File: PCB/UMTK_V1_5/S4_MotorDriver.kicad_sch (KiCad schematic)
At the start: 17 parts, among them J2 Motor Out, J3 Motor Shunt, U6 DRV8873SPWPRQ1

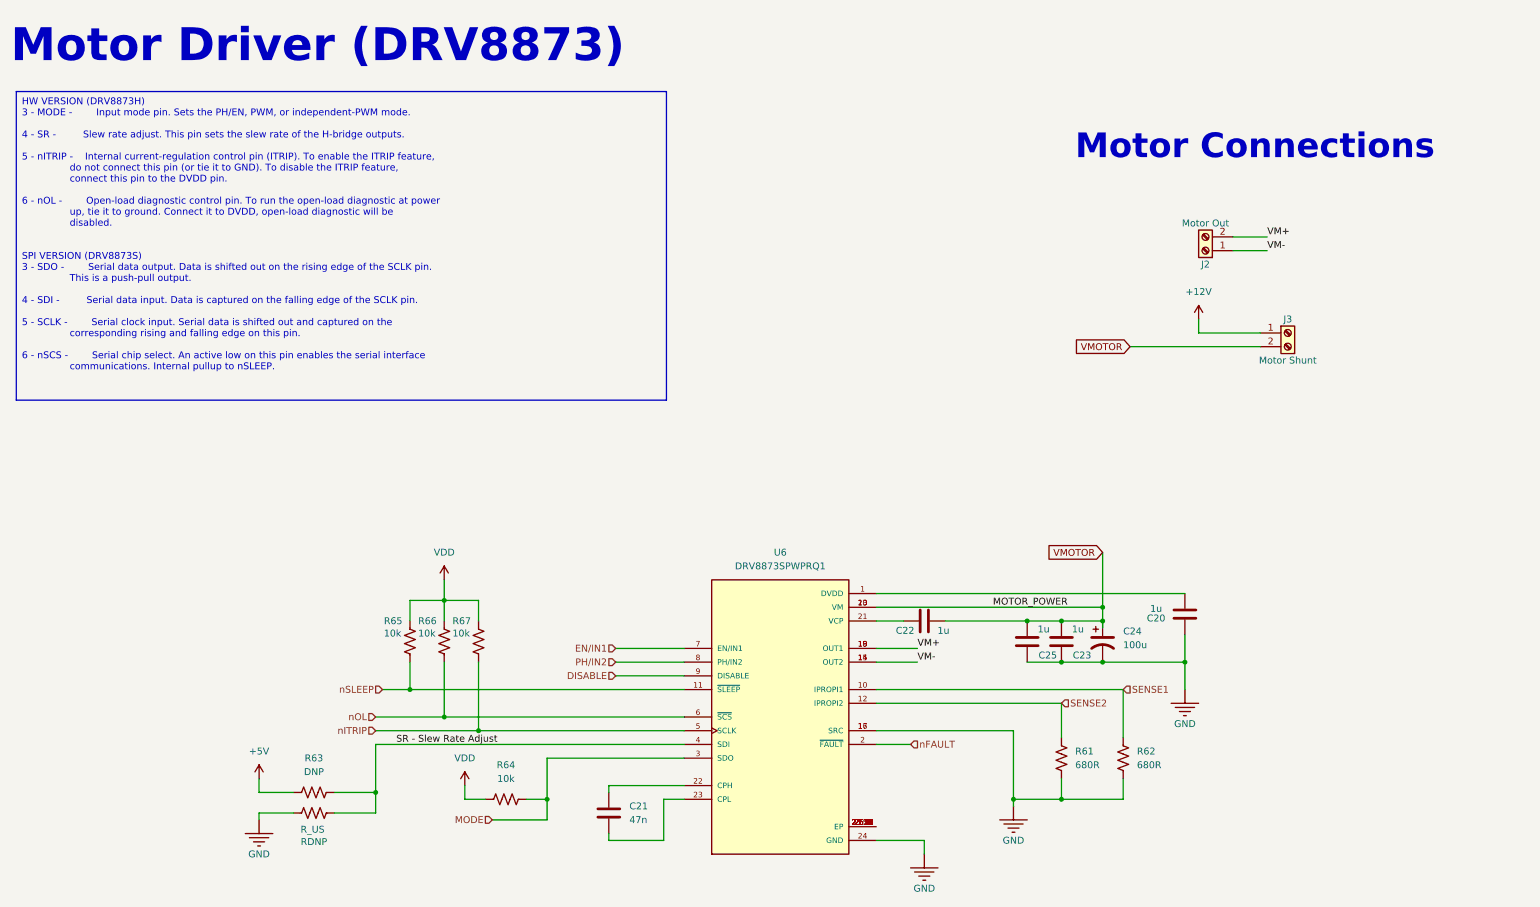
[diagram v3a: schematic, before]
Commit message: Schematic Done, Assigning footprint
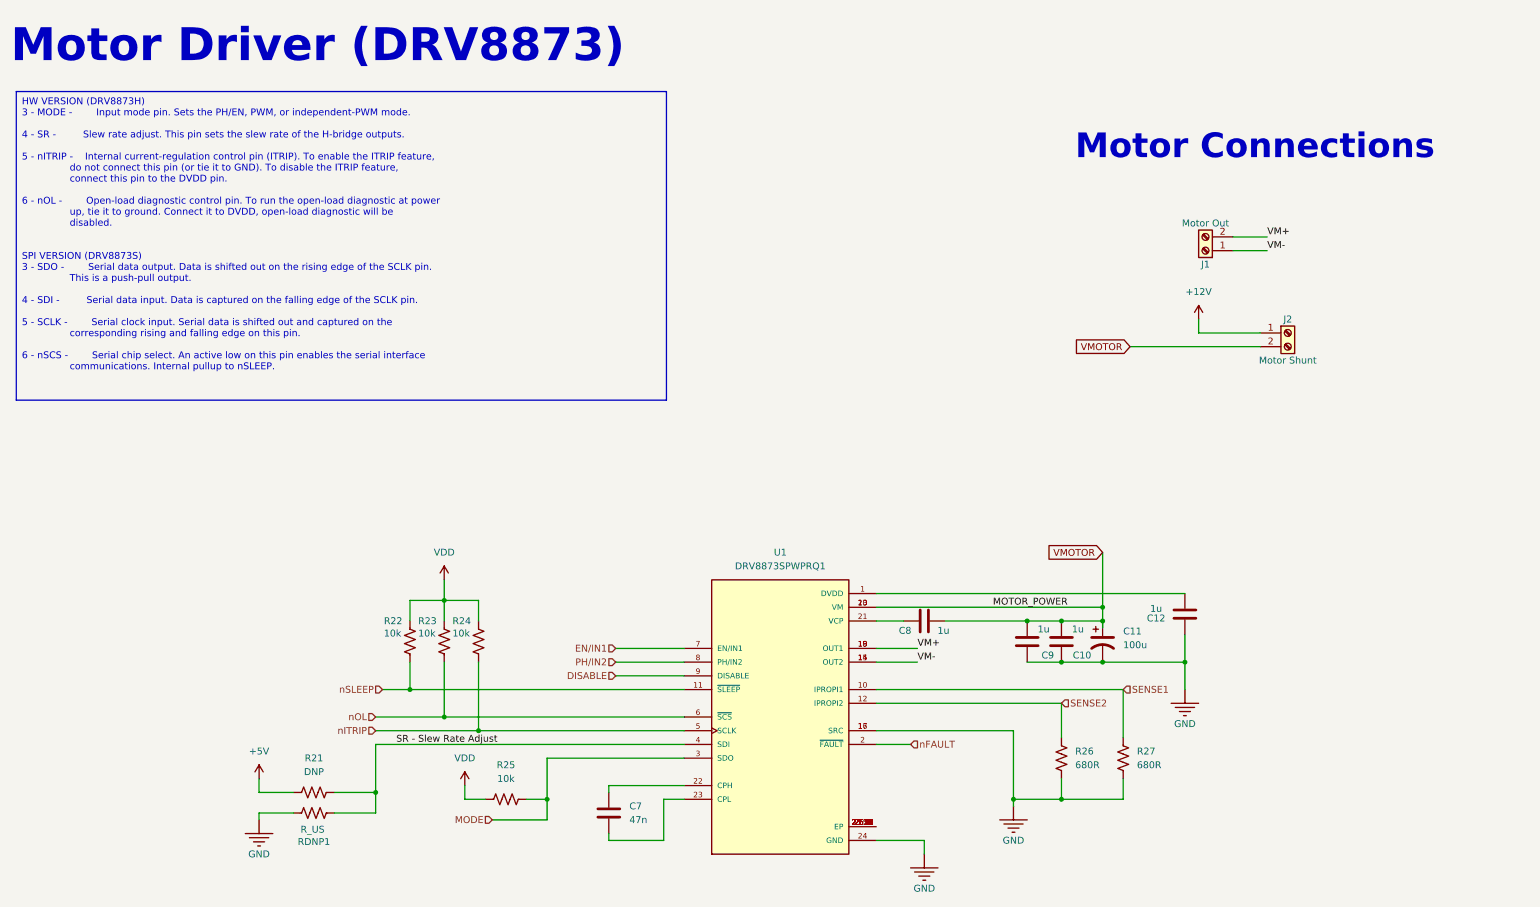
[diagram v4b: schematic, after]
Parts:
- renumbered C23 to C10, C24 to C11, C20 to C12, C21 to C7, C22 to C8, C25 to C9, J2 to J1, J3 to J2, R63 to R21, R65 to R22, R66 to R23, R67 to R24, R64 to R25, R61 to R26, R62 to R27, RDNP to RDNP1, U6 to U1
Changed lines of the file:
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@@
 		(dnp no)
 		(fields_autoplaced yes)
-		(property "Reference" "U6"
+		(property "Reference" "U1"
 			(at 156.21 110.49 0)
 			(effects
@@
 			(project ""
 				(path "/2bf3ea67-58b8-47b3-a768-ea6950b40edf/429db1c7-ec58-4147-903c-f97ceea1f1c2"
-					(reference "U6")
+					(reference "U1")
 					(unit 1)
 				)
@@
 		(dnp no)
 		(fields_autoplaced yes)
-		(property "Reference" "C21"
+		(property "Reference" "C7"
 			(at 128.27 157.4799 0)
 			(effects
@@
 			(project ""
 				(path "/2bf3ea67-58b8-47b3-a768-ea6950b40edf/429db1c7-ec58-4147-903c-f97ceea1f1c2"
-					(reference "C21")
+					(reference "C7")
 					(unit 1)
 				)
@@
 		(dnp no)
 		(fields_autoplaced yes)
-		(property "Reference" "R63"
+		(property "Reference" "R21"
 			(at 69.85 148.59 90)
 			(effects
@@
 			(project "UMTK"
 				(path "/2bf3ea67-58b8-47b3-a768-ea6950b40edf/429db1c7-ec58-4147-903c-f97ceea1f1c2"
-					(reference "R63")
+					(reference "R21")
 					(unit 1)
 				)
@@
 		(on_board yes)
 		(dnp no)
-		(property "Reference" "#PWR0160"
+		(property "Reference" "#PWR027"
 			(at 199.39 157.48 0)
 			(effects
@@
 			(project "UMTK"
 				(path "/2bf3ea67-58b8-47b3-a768-ea6950b40edf/429db1c7-ec58-4147-903c-f97ceea1f1c2"
-					(reference "#PWR0160")
+					(reference "#PWR027")
 					(unit 1)
 				)
@@
 		(dnp no)
 		(fields_autoplaced yes)
-		(property "Reference" "#PWR0140"
+		(property "Reference" "#PWR029"
 			(at 233.68 71.12 0)
 			(effects
@@
 			(project "UMTK"
 				(path "/2bf3ea67-58b8-47b3-a768-ea6950b40edf/429db1c7-ec58-4147-903c-f97ceea1f1c2"
-					(reference "#PWR0140")
+					(reference "#PWR029")
 					(unit 1)
 				)
@@
 		(on_board yes)
 		(dnp no)
-		(property "Reference" "C20"
+		(property "Reference" "C12"
 			(at 225.806 122.682 0)
 			(effects
@@
 			(project "UMTK"
 				(path "/2bf3ea67-58b8-47b3-a768-ea6950b40edf/429db1c7-ec58-4147-903c-f97ceea1f1c2"
-					(reference "C20")
+					(reference "C12")
 					(unit 1)
 				)
@@
 		(dnp no)
 		(fields_autoplaced yes)
-		(property "Reference" "R61"
+		(property "Reference" "R26"
 			(at 210.82 147.3199 0)
 			(effects
@@
 			(project ""
 				(path "/2bf3ea67-58b8-47b3-a768-ea6950b40edf/429db1c7-ec58-4147-903c-f97ceea1f1c2"
-					(reference "R61")
+					(reference "R26")
 					(unit 1)
 				)
@@
 		(on_board yes)
 		(dnp no)
-		(property "Reference" "J2"
+		(property "Reference" "J1"
 			(at 234.95 57.15 0)
 			(effects
@@
 			(project "UMTK"
 				(path "/2bf3ea67-58b8-47b3-a768-ea6950b40edf/429db1c7-ec58-4147-903c-f97ceea1f1c2"
-					(reference "J2")
+					(reference "J1")
 					(unit 1)
 				)
@@
 		(on_board yes)
 		(dnp no)
-		(property "Reference" "C25"
+		(property "Reference" "C9"
 			(at 205.74 129.54 0)
 			(effects
@@
 			(project "UMTK"
 				(path "/2bf3ea67-58b8-47b3-a768-ea6950b40edf/429db1c7-ec58-4147-903c-f97ceea1f1c2"
-					(reference "C25")
+					(reference "C9")
 					(unit 1)
 				)
@@
 		(dnp no)
 		(fields_autoplaced yes)
-		(property "Reference" "#PWR039"
+		(property "Reference" "#PWR024"
 			(at 93.98 119.38 0)
 			(effects
@@
 			(project ""
 				(path "/2bf3ea67-58b8-47b3-a768-ea6950b40edf/429db1c7-ec58-4147-903c-f97ceea1f1c2"
-					(reference "#PWR039")
+					(reference "#PWR024")
 					(unit 1)
 				)
@@
 		(dnp no)
 		(fields_autoplaced yes)
-		(property "Reference" "#PWR0162"
+		(property "Reference" "#PWR022"
 			(at 59.69 156.21 0)
 			(effects
@@
 			(project ""
 				(path "/2bf3ea67-58b8-47b3-a768-ea6950b40edf/429db1c7-ec58-4147-903c-f97ceea1f1c2"
-					(reference "#PWR0162")
+					(reference "#PWR022")
 					(unit 1)
 				)
@@
 		(on_board yes)
 		(dnp no)
-		(property "Reference" "C22"
+		(property "Reference" "C8"
 			(at 179.324 124.968 90)
 			(effects
@@
 			(project "UMTK"
 				(path "/2bf3ea67-58b8-47b3-a768-ea6950b40edf/429db1c7-ec58-4147-903c-f97ceea1f1c2"
-					(reference "C22")
+					(reference "C8")
 					(unit 1)
 				)
@@
 		(on_board yes)
 		(dnp no)
-		(property "Reference" "RDNP"
+		(property "Reference" "RDNP1"
 			(at 69.85 164.084 90)
 			(effects
@@
 			(project "UMTK"
 				(path "/2bf3ea67-58b8-47b3-a768-ea6950b40edf/429db1c7-ec58-4147-903c-f97ceea1f1c2"
-					(reference "RDNP")
+					(reference "RDNP1")
 					(unit 1)
 				)
@@
 		(on_board yes)
 		(dnp no)
-		(property "Reference" "C23"
+		(property "Reference" "C10"
 			(at 212.09 129.54 0)
 			(effects
@@
 			(project "UMTK"
 				(path "/2bf3ea67-58b8-47b3-a768-ea6950b40edf/429db1c7-ec58-4147-903c-f97ceea1f1c2"
-					(reference "C23")
+					(reference "C10")
 					(unit 1)
 				)
@@
 		(on_board yes)
 		(dnp no)
-		(property "Reference" "#PWR0158"
+		(property "Reference" "#PWR028"
 			(at 231.14 135.89 0)
 			(effects
@@
 			(project "UMTK"
 				(path "/2bf3ea67-58b8-47b3-a768-ea6950b40edf/429db1c7-ec58-4147-903c-f97ceea1f1c2"
-					(reference "#PWR0158")
+					(reference "#PWR028")
 					(unit 1)
 				)
@@
 		(on_board yes)
 		(dnp no)
-		(property "Reference" "#PWR0159"
+		(property "Reference" "#PWR026"
 			(at 182.88 166.37 0)
 			(effects
@@
 			(project "UMTK"
 				(path "/2bf3ea67-58b8-47b3-a768-ea6950b40edf/429db1c7-ec58-4147-903c-f97ceea1f1c2"
-					(reference "#PWR0159")
+					(reference "#PWR026")
 					(unit 1)
 				)
@@
 		(on_board yes)
 		(dnp no)
-		(property "Reference" "#PWR0161"
+		(property "Reference" "#PWR023"
 			(at 59.69 160.02 0)
 			(effects
@@
 			(project "UMTK"
 				(path "/2bf3ea67-58b8-47b3-a768-ea6950b40edf/429db1c7-ec58-4147-903c-f97ceea1f1c2"
-					(reference "#PWR0161")
+					(reference "#PWR023")
 					(unit 1)
 				)
@@
 		(on_board yes)
 		(dnp no)
-		(property "Reference" "R67"
+		(property "Reference" "R24"
 			(at 95.504 123.19 0)
 			(effects
@@
 			(project "UMTK"
 				(path "/2bf3ea67-58b8-47b3-a768-ea6950b40edf/429db1c7-ec58-4147-903c-f97ceea1f1c2"
-					(reference "R67")
+					(reference "R24")
 					(unit 1)
 				)
@@
 		(dnp no)
 		(fields_autoplaced yes)
-		(property "Reference" "R64"
+		(property "Reference" "R25"
 			(at 105.41 149.86 90)
 			(effects
@@
 			(project ""
 				(path "/2bf3ea67-58b8-47b3-a768-ea6950b40edf/429db1c7-ec58-4147-903c-f97ceea1f1c2"
-					(reference "R64")
+					(reference "R25")
 					(unit 1)
 				)
@@
 		(on_board yes)
 		(dnp no)
-		(property "Reference" "J3"
+		(property "Reference" "J2"
 			(at 250.19 67.31 0)
 			(effects
@@
 			(project "UMTK"
 				(path "/2bf3ea67-58b8-47b3-a768-ea6950b40edf/429db1c7-ec58-4147-903c-f97ceea1f1c2"
-					(reference "J3")
+					(reference "J2")
 					(unit 1)
 				)
@@
 		(on_board yes)
 		(dnp no)
-		(property "Reference" "R65"
+		(property "Reference" "R22"
 			(at 82.804 123.19 0)
 			(effects
@@
 			(project "UMTK"
 				(path "/2bf3ea67-58b8-47b3-a768-ea6950b40edf/429db1c7-ec58-4147-903c-f97ceea1f1c2"
-					(reference "R65")
+					(reference "R22")
 					(unit 1)
 				)
@@
 		(dnp no)
 		(fields_autoplaced yes)
-		(property "Reference" "R62"
+		(property "Reference" "R27"
 			(at 222.25 147.3199 0)
 			(effects
@@
 			(project "UMTK"
 				(path "/2bf3ea67-58b8-47b3-a768-ea6950b40edf/429db1c7-ec58-4147-903c-f97ceea1f1c2"
-					(reference "R62")
+					(reference "R27")
 					(unit 1)
 				)
@@
 		(dnp no)
 		(fields_autoplaced yes)
-		(property "Reference" "#PWR040"
+		(property "Reference" "#PWR025"
 			(at 97.79 157.48 0)
 			(effects
@@
 			(project ""
 				(path "/2bf3ea67-58b8-47b3-a768-ea6950b40edf/429db1c7-ec58-4147-903c-f97ceea1f1c2"
-					(reference "#PWR040")
+					(reference "#PWR025")
 					(unit 1)
 				)
@@
 		(dnp no)
 		(fields_autoplaced yes)
-		(property "Reference" "C24"
+		(property "Reference" "C11"
 			(at 219.71 125.0949 0)
 			(effects
@@
 			(project ""
 				(path "/2bf3ea67-58b8-47b3-a768-ea6950b40edf/429db1c7-ec58-4147-903c-f97ceea1f1c2"
-					(reference "C24")
+					(reference "C11")
 					(unit 1)
 				)
@@
 		(on_board yes)
 		(dnp no)
-		(property "Reference" "R66"
+		(property "Reference" "R23"
 			(at 89.154 123.19 0)
 			(effects
@@
 			(project "UMTK"
 				(path "/2bf3ea67-58b8-47b3-a768-ea6950b40edf/429db1c7-ec58-4147-903c-f97ceea1f1c2"
-					(reference "R66")
-					(unit 1)
-				)
+					(reference "R23")
+					(unit 1)
+				)

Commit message: Footprint assign
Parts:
- C10, C12, C8, C9: footprint (none) -> Diode_SMD:D_1206_3216Metric
- C11: footprint (none) -> Capacitor_SMD:CP_Elec_10x10.5
- C7: footprint (none) -> Capacitor_SMD:C_0402_1005Metric
- J1, J2: footprint (none) -> TerminalBlock_Altech:Altech_AK100_1x02_P5.00mm
- R21, R22, R23, R24, R25, RDNP1: footprint (none) -> Resistor_SMD:R_0402_1005Metric
- R26, R27: footprint (none) -> Resistor_SMD:R_0603_1608Metric
- U1: footprint DRV8873SPWPRQ1:IC_DRV8873SPWPRQ1 -> Package_SO:HTSSOP-24-1EP_4.4x7.8mm_P0.65mm_EP3.4x7.8mm_Mask2.4x2.98mm_ThermalVias
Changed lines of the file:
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@@
 			)
 		)
-		(property "Footprint" "DRV8873SPWPRQ1:IC_DRV8873SPWPRQ1"
+		(property "Footprint" "Package_SO:HTSSOP-24-1EP_4.4x7.8mm_P0.65mm_EP3.4x7.8mm_Mask2.4x2.98mm_ThermalVias"
 			(at 156.21 140.97 0)
 			(effects
@@
 			)
 		)
-		(property "Footprint" ""
+		(property "Footprint" "Capacitor_SMD:C_0402_1005Metric"
 			(at 125.4252 162.56 0)
 			(effects
@@
 			)
 		)
-		(property "Footprint" ""
+		(property "Footprint" "Resistor_SMD:R_0402_1005Metric"
 			(at 69.596 155.956 90)
 			(effects
@@
 			)
 		)
-		(property "Footprint" ""
+		(property "Footprint" "Diode_SMD:D_1206_3216Metric"
 			(at 232.1052 125.73 0)
 			(effects
@@
 			)
 		)
-		(property "Footprint" ""
+		(property "Footprint" "Resistor_SMD:R_0603_1608Metric"
 			(at 207.264 148.336 90)
 			(effects
@@
 			)
 		)
-		(property "Footprint" ""
+		(property "Footprint" "TerminalBlock_Altech:Altech_AK100_1x02_P5.00mm"
 			(at 234.95 54.61 0)
 			(effects
@@
 			)
 		)
-		(property "Footprint" ""
+		(property "Footprint" "Diode_SMD:D_1206_3216Metric"
 			(at 200.9648 123.19 0)
 			(effects
@@
 			)
 		)
-		(property "Footprint" ""
+		(property "Footprint" "Diode_SMD:D_1206_3216Metric"
 			(at 186.69 122.2248 0)
 			(effects
@@
 			)
 		)
-		(property "Footprint" ""
+		(property "Footprint" "Resistor_SMD:R_0402_1005Metric"
 			(at 70.104 157.734 90)
 			(effects
@@
 			)
 		)
-		(property "Footprint" ""
+		(property "Footprint" "Diode_SMD:D_1206_3216Metric"
 			(at 207.3148 123.19 0)
 			(effects
@@
 			)
 		)
-		(property "Footprint" ""
+		(property "Footprint" "Resistor_SMD:R_0402_1005Metric"
 			(at 99.314 126.746 90)
 			(effects
@@
 			)
 		)
-		(property "Footprint" ""
+		(property "Footprint" "Resistor_SMD:R_0402_1005Metric"
 			(at 105.664 155.194 90)
 			(effects
@@
 			)
 		)
-		(property "Footprint" ""
+		(property "Footprint" "TerminalBlock_Altech:Altech_AK100_1x02_P5.00mm"
 			(at 250.19 69.85 0)
 			(effects
@@
 			)
 		)
-		(property "Footprint" ""
+		(property "Footprint" "Resistor_SMD:R_0402_1005Metric"
 			(at 86.614 126.746 90)
 			(effects
@@
 			)
 		)
-		(property "Footprint" ""
+		(property "Footprint" "Resistor_SMD:R_0603_1608Metric"
 			(at 218.694 148.336 90)
 			(effects
@@
 			)
 		)
-		(property "Footprint" ""
+		(property "Footprint" "Capacitor_SMD:CP_Elec_10x10.5"
 			(at 215.9 127 0)
 			(effects
@@
 			)
 		)
-		(property "Footprint" ""
+		(property "Footprint" "Resistor_SMD:R_0402_1005Metric"
 			(at 92.964 126.746 90)
 			(effects

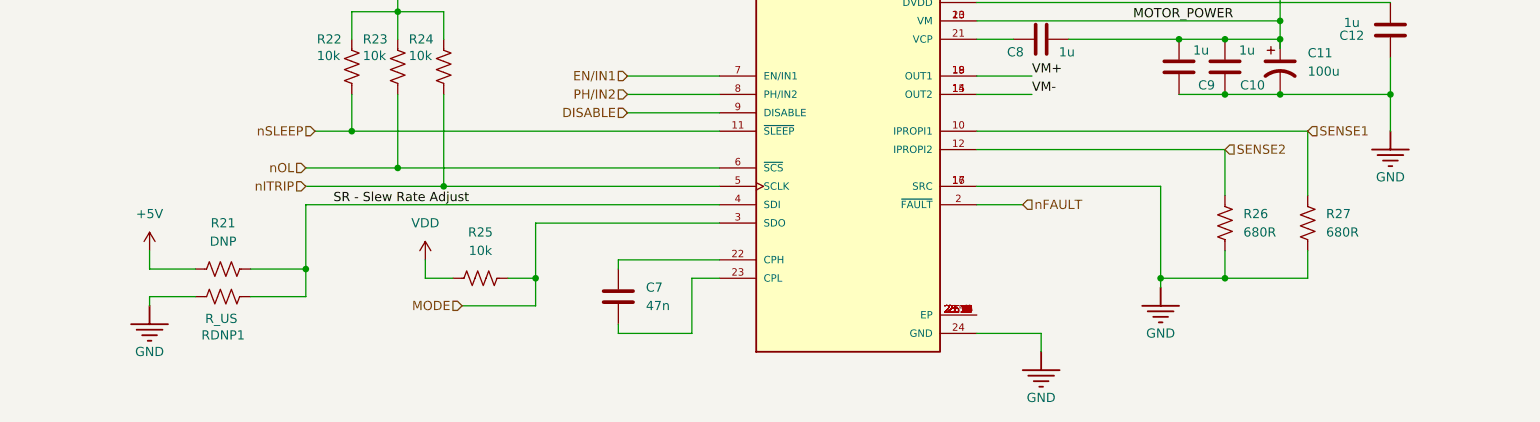
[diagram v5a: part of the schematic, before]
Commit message: ERC good, imported into PCB
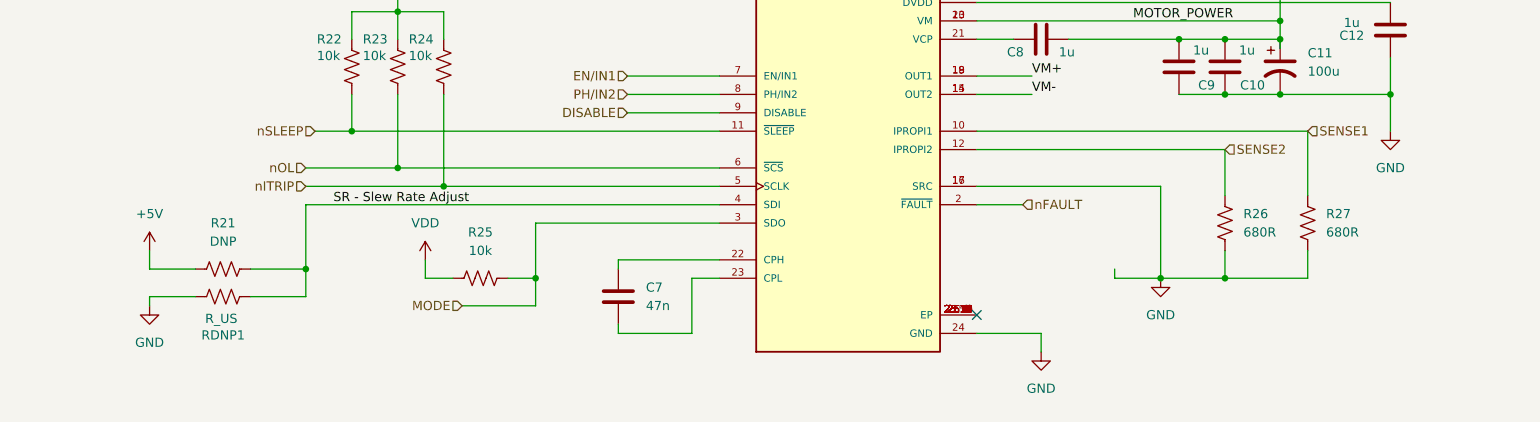
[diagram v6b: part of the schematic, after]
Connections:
- no-connect marks 0 -> 1
